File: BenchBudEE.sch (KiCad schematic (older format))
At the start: 0 parts

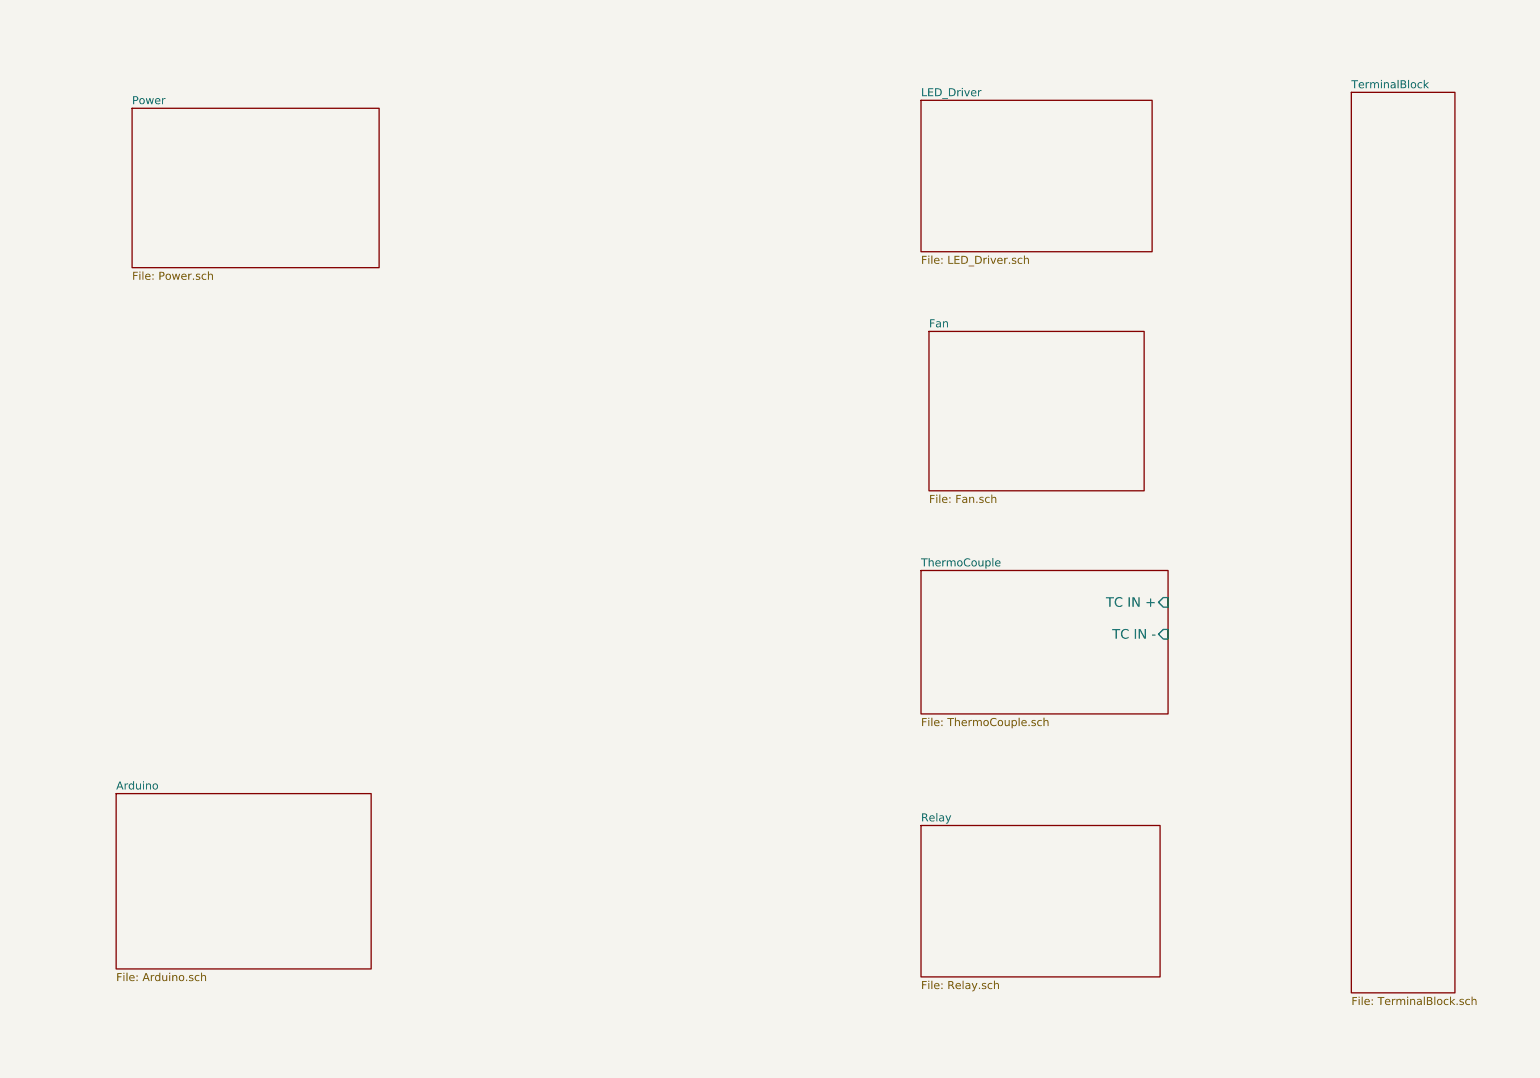
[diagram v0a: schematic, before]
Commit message: create inputs and outputs for main modules
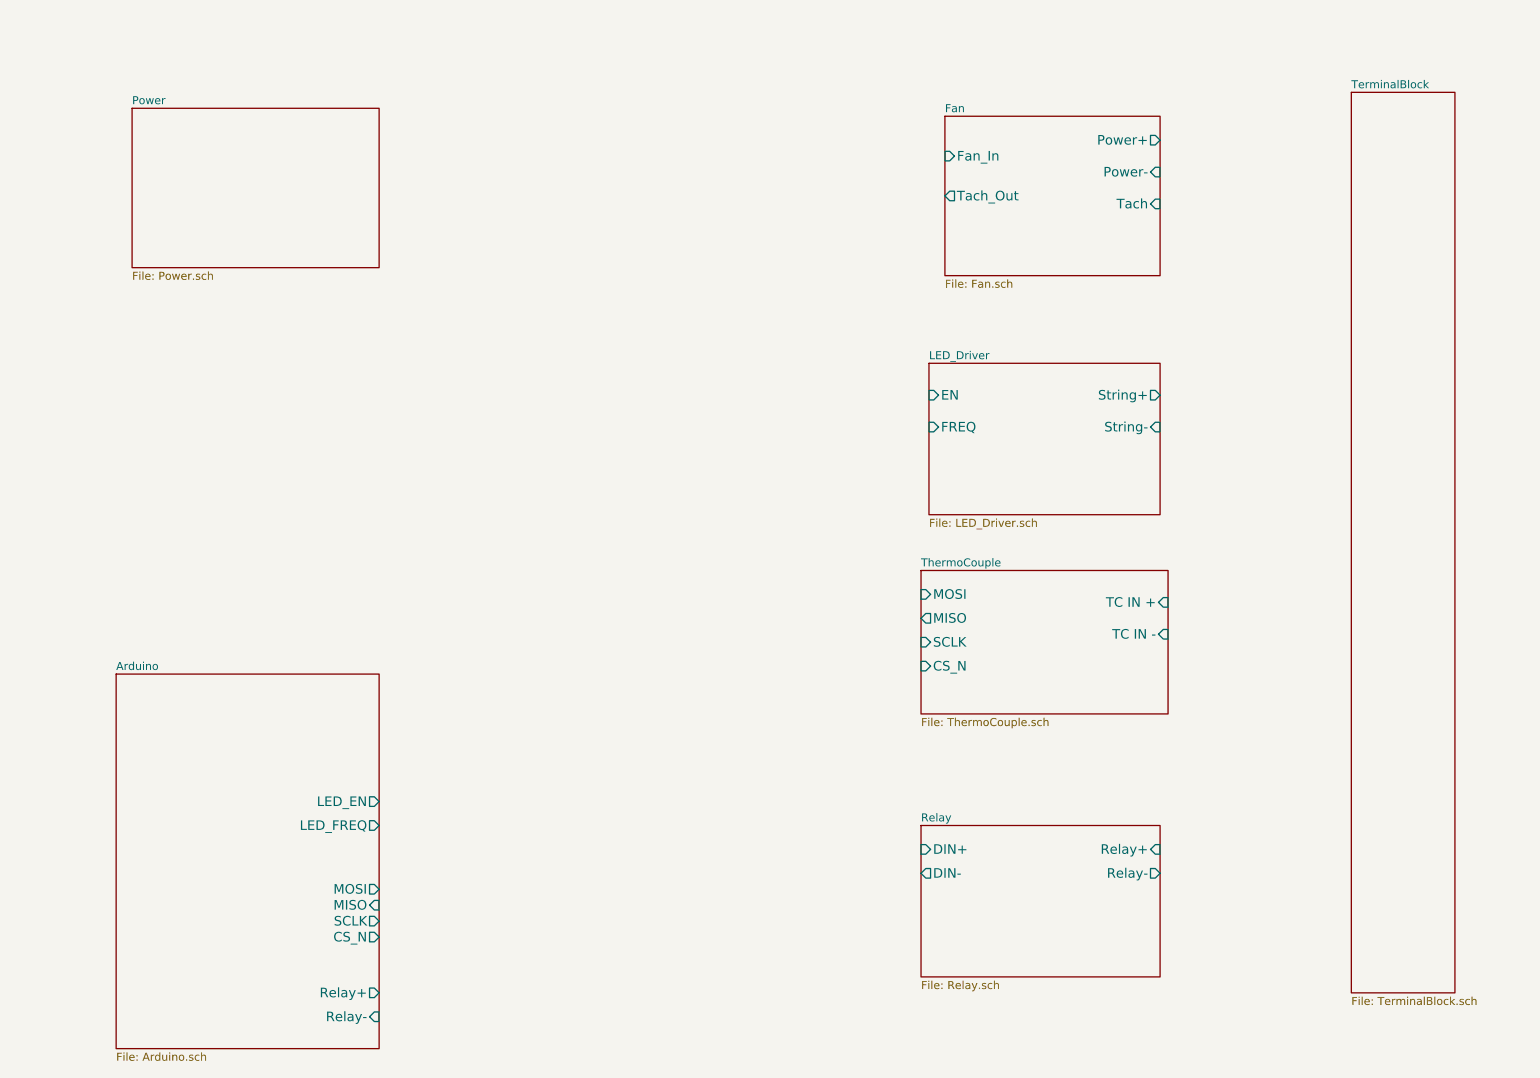
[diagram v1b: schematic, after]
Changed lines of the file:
@@
 $EndDescr
 $Sheet
-S 2200 5500 1600 1100
+S 2200 4750 1650 2350
 U 52ED1A8D
 F0 "Arduino" 50
 F1 "Arduino.sch" 50
+F2 "Relay+" O R 3850 6750 60
+F3 "Relay-" I R 3850 6900 60
+F4 "MOSI" O R 3850 6100 60
+F5 "MISO" I R 3850 6200 60
+F6 "SCLK" O R 3850 6300 60
+F7 "CS_N" O R 3850 6400 60
+F8 "LED_EN" O R 3850 5550 60
+F9 "LED_FREQ" O R 3850 5700 60
 $EndSheet
 $Sheet
@@
 F2 "TC IN +" I R 8800 4300 60
 F3 "TC IN -" I R 8800 4500 60
+F4 "MOSI" I L 7250 4250 60
+F5 "MISO" O L 7250 4400 60
+F6 "SCLK" I L 7250 4550 60
+F7 "CS_N" I L 7250 4700 60
 $EndSheet
 $Sheet
@@
 F0 "Relay" 50
 F1 "Relay.sch" 50
+F2 "DIN+" I L 7250 5850 60
+F3 "DIN-" O L 7250 6000 60
+F4 "Relay+" I R 8750 5850 60
+F5 "Relay-" O R 8750 6000 60
 $EndSheet
 $Sheet
@@
 $EndSheet
 $Sheet
-S 7250 1150 1450 950
+S 7300 2800 1450 950
 U 52ED1B6A
 F0 "LED_Driver" 50
 F1 "LED_Driver.sch" 50
+F2 "EN" I L 7300 3000 60
+F3 "FREQ" I L 7300 3200 60
+F4 "String+" O R 8750 3000 60
+F5 "String-" I R 8750 3200 60
 $EndSheet
 $Sheet
-S 7300 2600 1350 1000
+S 7400 1250 1350 1000
 U 52ED1BE8
 F0 "Fan" 50
 F1 "Fan.sch" 50
+F2 "Power+" O R 8750 1400 60
+F3 "Power-" I R 8750 1600 60
+F4 "Tach" I R 8750 1800 60
+F5 "Tach_Out" O L 7400 1750 60
+F6 "Fan_In" I L 7400 1500 60
 $EndSheet
 $Sheet

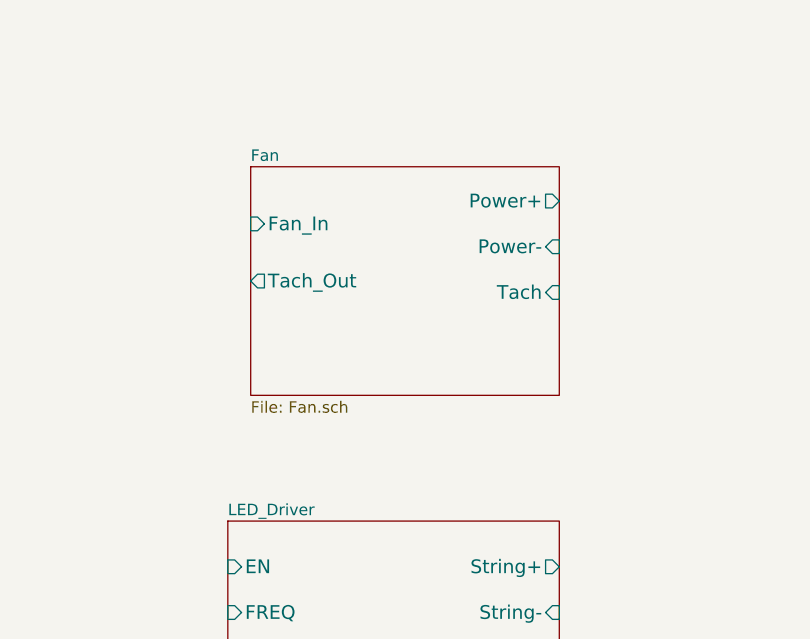
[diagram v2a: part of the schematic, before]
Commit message: Added Fan control outline
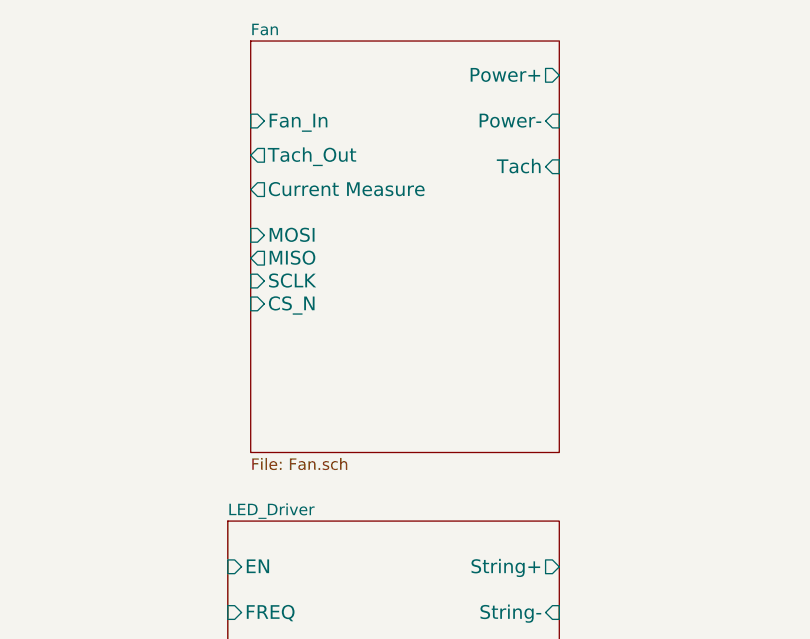
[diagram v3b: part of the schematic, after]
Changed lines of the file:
@@
 $EndSheet
 $Sheet
-S 7400 1250 1350 1000
+S 7400 700  1350 1800
 U 52ED1BE8
 F0 "Fan" 50
 F1 "Fan.sch" 50
-F2 "Power+" O R 8750 1400 60
-F3 "Power-" I R 8750 1600 60
-F4 "Tach" I R 8750 1800 60
-F5 "Tach_Out" O L 7400 1750 60
-F6 "Fan_In" I L 7400 1500 60
+F2 "Power+" O R 8750 850 60
+F3 "Power-" I R 8750 1050 60
+F4 "Tach" I R 8750 1250 60
+F5 "Tach_Out" O L 7400 1200 60
+F6 "Fan_In" I L 7400 1050 60
+F7 "MOSI" I L 7400 1550 60
+F8 "MISO" O L 7400 1650 60
+F9 "SCLK" I L 7400 1750 60
+F10 "CS_N" I L 7400 1850 60
+F11 "Current Measure" O L 7400 1350 60
 $EndSheet
 $Sheet

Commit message: Added Power Module outline
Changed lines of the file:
@@
 $Descr A4 11693 8268
 encoding utf-8
-Sheet 1 8
+Sheet 1 9
 Title ""
 Date "3 feb 2014"
@@
 $EndSheet
 $Sheet
-S 2300 1200 1550 1000
+S 1550 1200 1550 1000
 U 52ED1B32
 F0 "Power" 50
@@
 F1 "TerminalBlock.sch" 50
 $EndSheet
+$Sheet
+S 4150 1150 1600 1000
+U 52EFCF2A
+F0 "PowerAdjustmentMonitor" 50
+F1 "PowerAdjustmentMonitor.sch" 50
+$EndSheet
 $EndSCHEMATC
